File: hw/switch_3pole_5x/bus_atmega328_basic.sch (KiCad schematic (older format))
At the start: 26 parts, among them J12 CONN-ISP-6, J13 WAGO 243-723, J14 WAGO 243-724, J15 WAGO 243-721, J16 WAGO 243-722, U3 25LC256, U4 ATMEGA328-TQFP32, U5 7,3728MHz, U6 MAX487ECSA, U7 AM1S-2405

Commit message: Added LED and testpoints
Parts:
- added J24: tp_cseep, Connector_Miscelleaneus:Testpoint_1mm, symbol connectors:CONN_1
- added J25: tp_miso, Connector_Miscelleaneus:Testpoint_1mm, symbol connectors:CONN_1
- added J26: tp_mosi, Connector_Miscelleaneus:Testpoint_1mm, symbol connectors:CONN_1
- added J27: tp_sck, Connector_Miscelleaneus:Testpoint_1mm, symbol connectors:CONN_1
- added J28: tp_txden, Connector_Miscelleaneus:Testpoint_1mm, symbol connectors:CONN_1
- added J29: tp_txd, Connector_Miscelleaneus:Testpoint_1mm, symbol connectors:CONN_1
- added J30: tp_rxd, Connector_Miscelleaneus:Testpoint_1mm, symbol connectors:CONN_1
- added J31: tp_vcc, Connector_Miscelleaneus:Testpoint_1mm, symbol connectors:CONN_1
- added J32: tp_gnd, Connector_Miscelleaneus:Testpoint_1mm, symbol connectors:CONN_1
- C3, C4, C5, C6, C7, C8, C9: symbol C -> switch_3pole_5x-rescue:C
- D22: symbol SEMTECH_SR05 -> switch_3pole_5x-rescue:SEMTECH_SR05
- F2: symbol FUSE -> switch_3pole_5x-rescue:FUSE
- J12: symbol CONN-ISP-6 -> switch_3pole_5x-rescue:CONN-ISP-6
- J13, J14, J15, J16: symbol CONN_1 -> switch_3pole_5x-rescue:CONN_1
- LOGO4: symbol OPEN_HARDWARE_1 -> switch_3pole_5x-rescue:OPEN_HARDWARE_1
- R31, R32, R33, R34, R35, R36: symbol R -> switch_3pole_5x-rescue:R
- U3: symbol 25LCXXX -> switch_3pole_5x-rescue:25LCXXX
- U4: symbol ATMEGA88-TQFP32 -> switch_3pole_5x-rescue:ATMEGA88-TQFP32
- U5: symbol CRYSTAL -> switch_3pole_5x-rescue:CRYSTAL
- U6: symbol MAX487 -> switch_3pole_5x-rescue:MAX487
- U7: symbol AM1S-2403 -> switch_3pole_5x-rescue:AM1S-2403
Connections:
- net /CSEEP: now also J24.1
- net GND: now also J32.1
- net MISO: now also J25.1
- net MOSI: now also J26.1
- net RXD0: now also J30.1
- net SCK: now also J27.1
- net TXD0: now also J29.1
- net TXD0EN: now also J28.1
- net VCC: now also J31.1

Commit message: fixed switch_3pole_5x library references added component placement drawings updated 3d images and gerber files
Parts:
- C3, C4, C5, C6, C7, C8, C9: symbol switch_3pole_5x-rescue:C -> standard:C
- D22: symbol switch_3pole_5x-rescue:SEMTECH_SR05 -> diodes:SEMTECH_SR05
- F2: symbol switch_3pole_5x-rescue:FUSE -> standard:FUSE
- J12: symbol switch_3pole_5x-rescue:CONN-ISP-6 -> connectors:CONN-ISP-6
- J13, J14, J15, J16: symbol switch_3pole_5x-rescue:CONN_1 -> connectors:CONN_1
- LOGO4: symbol switch_3pole_5x-rescue:OPEN_HARDWARE_1 -> logo:OPEN_HARDWARE_1
- R31, R32, R33, R34, R35, R36: symbol switch_3pole_5x-rescue:R -> standard:R
- U3: symbol switch_3pole_5x-rescue:25LCXXX -> ics_peripheral:25LCXXX
- U4: symbol switch_3pole_5x-rescue:ATMEGA88-TQFP32 -> ics_controller_atmel:ATMEGA88-TQFP32
- U5: symbol switch_3pole_5x-rescue:CRYSTAL -> standard:CRYSTAL
- U6: symbol switch_3pole_5x-rescue:MAX487 -> ics_misc:MAX487
- U7: symbol switch_3pole_5x-rescue:AM1S-2403 -> ics_regulator:AM1S-2405
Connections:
- net at C6.1, U4.8 (PB7/XTAL2): no longer U5.2
- net at C5.1, U4.7 (PB6/XTAL1): no longer U5.1
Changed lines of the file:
@@
 Title "switch 3pole (bus_atmega328_basic)"
 Date "2018-09-18"
-Rev "1"
+Rev "A"
 Comp "KoeWiBa"
 Comment1 ""
@@
 $EndDescr
 $Comp
-L switch_3pole_5x-rescue:25LCXXX U3
+L ics_peripheral:25LCXXX U3
 U 1 1 559D5893
 P 5200 6850
@@
 $EndComp
 $Comp
-L switch_3pole_5x-rescue:MAX487 U6
+L ics_misc:MAX487 U6
 U 1 1 559D596F
 P 7600 2850
@@
 $EndComp
 $Comp
-L switch_3pole_5x-rescue:CONN_1 J13
+L connectors:CONN_1 J13
 U 1 1 559D5A6B
 P 10150 2500
@@
 $EndComp
 $Comp
-L switch_3pole_5x-rescue:CONN_1 J14
+L connectors:CONN_1 J14
 U 1 1 559D5ACC
 P 10150 2700
@@
 $EndComp
 $Comp
-L switch_3pole_5x-rescue:CONN_1 J15
+L connectors:CONN_1 J15
 U 1 1 559D5B5B
 P 10150 2900
@@
 $EndComp
 $Comp
-L switch_3pole_5x-rescue:CONN_1 J16
+L connectors:CONN_1 J16
 U 1 1 559D5B94
 P 10150 3100
@@
 $EndComp
 $Comp
-L switch_3pole_5x-rescue:AM1S-2403 U7
+L ics_regulator:AM1S-2405 U7
 U 1 1 559D5CD1
 P 8050 1300
@@
 $EndComp
 $Comp
-L switch_3pole_5x-rescue:C C9
+L standard:C C9
 U 1 1 559D5E5A
 P 7800 2200
@@
 $EndComp
 $Comp
-L switch_3pole_5x-rescue:C C3
+L standard:C C3
 U 1 1 559D623B
 P 4950 1800
@@
 $EndComp
 $Comp
-L switch_3pole_5x-rescue:C C6
+L standard:C C6
 U 1 1 559D6400
 P 6450 4650
@@
 $EndComp
 $Comp
-L switch_3pole_5x-rescue:C C5
+L standard:C C5
 U 1 1 559D67BD
 P 6450 4300
@@
 $EndComp
 $Comp
-L switch_3pole_5x-rescue:C C4
+L standard:C C4
 U 1 1 559D6AC5
 P 5200 6350
@@
 $EndComp
 $Comp
-L switch_3pole_5x-rescue:CONN-ISP-6 J12
+L connectors:CONN-ISP-6 J12
 U 1 1 559D6B4E
 P 7600 5600
@@
 $EndComp
 $Comp
-L switch_3pole_5x-rescue:CRYSTAL U5
+L standard:CRYSTAL U5
 U 1 1 559D6E2A
 P 6300 4300
@@
 $EndComp
 $Comp
-L switch_3pole_5x-rescue:GND #PWR029
+L power:GND #PWR029
 U 1 1 559D7329
 P 5350 4950
@@
 $EndComp
 $Comp
-L switch_3pole_5x-rescue:GND #PWR030
+L power:GND #PWR030
 U 1 1 559D76CD
 P 4550 7100
@@
 $EndComp
 $Comp
-L power1:+24V #PWR031
+L power:+24V #PWR031
 U 1 1 559D77F1
 P 9350 2400
@@
 $EndComp
 $Comp
-L switch_3pole_5x-rescue:R R34
+L standard:R R34
 U 1 1 559D7BAA
 P 4900 5700
@@
 $EndComp
 $Comp
-L switch_3pole_5x-rescue:R R33
+L standard:R R33
 U 1 1 559D7C90
 P 4900 5600
@@
 $EndComp
 $Comp
-L switch_3pole_5x-rescue:R R32
+L standard:R R32
 U 1 1 559D7D33
 P 4900 5500
@@
 Connection ~ 7600 2200
 $Comp
-L switch_3pole_5x-rescue:GND #PWR032
+L power:GND #PWR032
 U 1 1 55A00C4E
 P 7600 3450
@@
 	8100 2700 8750 2700
 $Comp
-L switch_3pole_5x-rescue:GND #PWR033
+L power:GND #PWR033
 U 1 1 55A03238
 P 4950 2100
@@
 SCK
 $Comp
-L switch_3pole_5x-rescue:R R31
+L standard:R R31
 U 1 1 55A05C69
 P 4550 6400
@@
 $EndComp
 $Comp
-L switch_3pole_5x-rescue:R R35
+L standard:R R35
 U 1 1 55A05DA4
 P 5900 6400
@@
 	5750 7000 5950 7000
 $Comp
-L switch_3pole_5x-rescue:GND #PWR034
+L power:GND #PWR034
 U 1 1 55A076FA
 P 5200 6500
@@
 PB4_MISO
 $Comp
-L switch_3pole_5x-rescue:GND #PWR035
+L power:GND #PWR035
 U 1 1 55A08693
 P 8000 5800
@@
 	7300 5700 6850 5700
 $Comp
-L switch_3pole_5x-rescue:GND #PWR036
+L power:GND #PWR036
 U 1 1 55A0C631
 P 8000 2300
@@
 	8000 2200 8000 2300
 $Comp
-L switch_3pole_5x-rescue:C C7
+L standard:C C7
 U 1 1 55A0D462
 P 6550 2250
@@
 	6550 2350 6550 2450
 $Comp
-L switch_3pole_5x-rescue:R R36
+L standard:R R36
 U 1 1 55A0DE32
 P 6550 1750
@@
 Connection ~ 6550 2050
 $Comp
-L switch_3pole_5x-rescue:GND #PWR037
+L power:GND #PWR037
 U 1 1 55A0E9DD
 P 6550 2450
@@
 	7200 1400 7200 1500
 $Comp
-L power1:+24V #PWR038
+L power:+24V #PWR038
 U 1 1 55A0FF09
 P 8650 1100
@@
 $EndComp
 $Comp
-L switch_3pole_5x-rescue:GND #PWR039
+L power:GND #PWR039
 U 1 1 55A10203
 P 8650 1500
@@
 $EndComp
 $Comp
-L switch_3pole_5x-rescue:GND #PWR040
+L power:GND #PWR040
 U 1 1 55A10383
 P 7200 1600
@@
 $EndComp
 $Comp
-L switch_3pole_5x-rescue:GND #PWR041
+L power:GND #PWR041
 U 1 1 55A105FF
 P 9550 4200
@@
 PB3_MOSI
 $Comp
-L switch_3pole_5x-rescue:OPEN_HARDWARE_1 LOGO4
+L logo:OPEN_HARDWARE_1 LOGO4
 U 1 1 55B4D774
 P 1300 7350
@@
 	2775 4300 2875 4400
 $Comp
-L switch_3pole_5x-rescue:GND #PWR042
+L power:GND #PWR042
 U 1 1 55D48C16
 P 1800 3700
@@
 PD7
 $Comp
-L switch_3pole_5x-rescue:ATMEGA88-TQFP32 U4
+L ics_controller_atmel:ATMEGA88-TQFP32 U4
 U 1 1 55D48DEF
 P 5350 3550
@@
 	6200 3950 6200 4650
 Wire Wire Line
-	6200 4650 6300 4650
-Connection ~ 6300 4650
-Wire Wire Line
-	6250 4300 6300 4300
-Wire Wire Line
 	6250 4300 6250 3850
 Wire Wire Line
 	6250 3850 6150 3850
-Connection ~ 6300 4300
 Wire Wire Line
 	6550 4300 6650 4300
@@
 	1500 5800 4200 5800
 $Comp
-L switch_3pole_5x-rescue:SEMTECH_SR05 D22
+L diodes:SEMTECH_SR05 D22
 U 1 1 55EC2FF2
 P 9050 3700
@@
 	4950 1900 4950 2100
 $Comp
-L power1:VCC #PWR043
+L power:VCC #PWR043
 U 1 1 5605057B
 P 7200 1000
@@
 $EndComp
 $Comp
-L power1:VCC #PWR044
+L power:VCC #PWR044
 U 1 1 560505CB
 P 5250 1400
@@
 $EndComp
 $Comp
-L power1:VCC #PWR045
+L power:VCC #PWR045
 U 1 1 5605061B
 P 7600 2100
@@
 $EndComp
 $Comp
-L power1:VCC #PWR046
+L power:VCC #PWR046
 U 1 1 560506A7
 P 5200 6050
@@
 $EndComp
 $Comp
-L power1:VCC #PWR047
+L power:VCC #PWR047
 U 1 1 56050805
 P 1800 3800
@@
 $EndComp
 $Comp
-L power1:VCC #PWR048
+L power:VCC #PWR048
 U 1 1 5605145B
 P 8000 5400
@@
 B
 $Comp
-L switch_3pole_5x-rescue:FUSE F2
+L standard:FUSE F2
 U 1 1 56648405
 P 9750 2500
@@
 SCK
 $Comp
-L power1:+24V #PWR049
+L power:+24V #PWR049
 U 1 1 578A4CD7
 P 2775 2575
@@
 	2775 2575 2475 2575
 $Comp
-L switch_3pole_5x-rescue:C C8
+L standard:C C8
 U 1 1 578E4351
 P 7200 1300
@@
 	5350 4850 5350 4950
 Wire Wire Line
-	6300 4650 6350 4650
-Wire Wire Line
-	6300 4300 6350 4300
-Wire Wire Line
 	5450 4850 6650 4850
 Wire Wire Line
@@
 Wire Wire Line
 	7100 2700 7100 2550
-Connection ~ 7100 2700
 Wire Wire Line
 	7100 3000 7100 3150
-Connection ~ 7100 3000
 $Comp
 L connectors:CONN_1 J31
@@
 Wire Wire Line
 	3700 7000 4100 7000
+Wire Wire Line
+	6200 4650 6350 4650
+Wire Wire Line
+	6250 4300 6350 4300
 Wire Bus Line
 	5400 5600 5400 5800

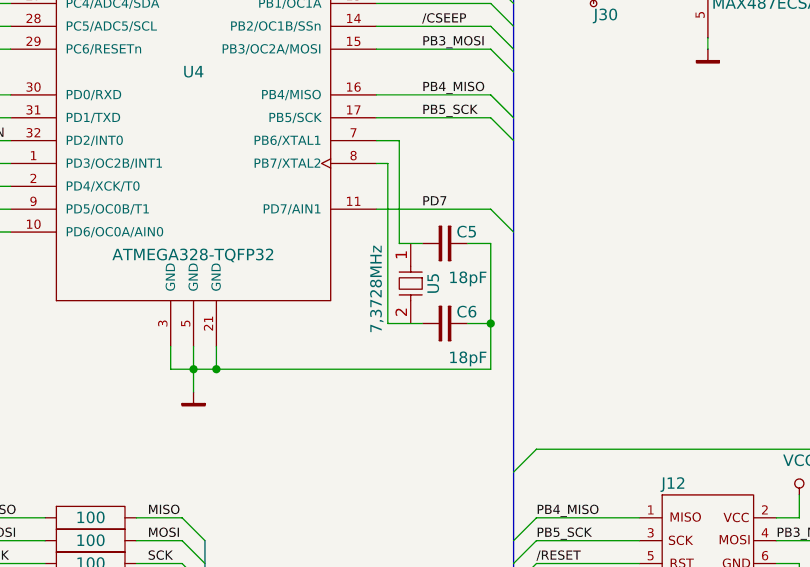
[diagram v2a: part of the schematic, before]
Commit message: Update to revision B. Fix footprint of U4 (TQFP32)
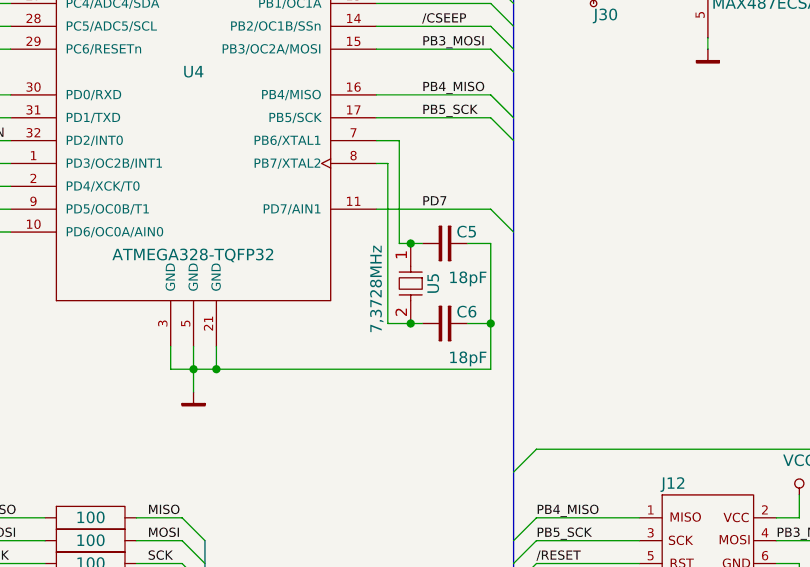
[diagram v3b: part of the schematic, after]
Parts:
- U4: footprint Housings_QFP:TQFP-44_10x10mm_Pitch0.8mm -> Housings_QFP:TQFP-32_7x7mm_Pitch0.8mm
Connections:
- net at C6.1, U4.8 (PB7/XTAL2): now also U5.2
- net at C5.1, U4.7 (PB6/XTAL1): now also U5.1
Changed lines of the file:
@@
 Sheet 4 4
 Title "switch 3pole (bus_atmega328_basic)"
-Date "2018-09-18"
-Rev "A"
+Date "2018-12-27"
+Rev "B"
 Comp "KoeWiBa"
 Comment1 ""
@@
 F 0 "U4" H 5350 3550 50  0000 C CNN
 F 1 "ATMEGA328-TQFP32" H 5350 2750 50  0000 C CNN
-F 2 "Housings_QFP:TQFP-44_10x10mm_Pitch0.8mm" H 5350 3550 25  0001 C CNN
+F 2 "Housings_QFP:TQFP-32_7x7mm_Pitch0.8mm" H 5350 3550 25  0001 C CNN
 F 3 "DOCUMENTATION" H 5350 3550 25  0001 C CNN
 	1    5350 3550
@@
 	3700 7000 4100 7000
 Wire Wire Line
-	6200 4650 6350 4650
-Wire Wire Line
-	6250 4300 6350 4300
+	6200 4650 6300 4650
+Wire Wire Line
+	6250 4300 6300 4300
 Wire Bus Line
 	5400 5600 5400 5800
@@
 Wire Bus Line
 	4200 2950 4200 5800
+Connection ~ 6300 4300
+Wire Wire Line
+	6300 4300 6350 4300
+Connection ~ 6300 4650
+Wire Wire Line
+	6300 4650 6350 4650
 $EndSCHEMATC
